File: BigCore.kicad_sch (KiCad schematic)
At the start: 4 parts

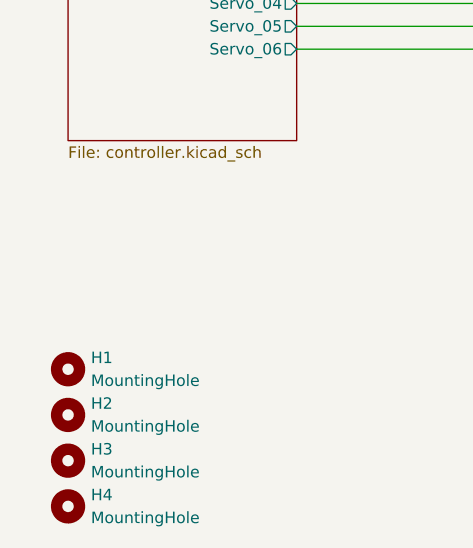
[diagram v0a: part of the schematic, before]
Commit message: Changed the WS2812 driver IC Optimized the Analog GND and AVCC routing Changed RS485 driver Removed TVS Diode at the RS485 driver (already has 15kV rating)
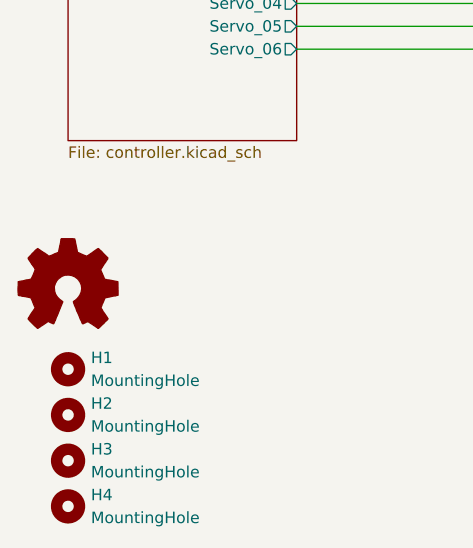
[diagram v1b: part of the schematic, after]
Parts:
- added H5: Logo_Open_Hardware_Small, Symbol:OSHW-Logo_5.7x6mm_SilkScreen, symbol Graphic:Logo_Open_Hardware_Small
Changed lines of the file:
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@@
+	)
+	(symbol
+		(lib_id "Graphic:Logo_Open_Hardware_Small")
+		(at 38.1 156.21 0)
+		(unit 1)
+		(exclude_from_sim no)
+		(in_bom no)
+		(on_board yes)
+		(dnp no)
+		(fields_autoplaced yes)
+		(property "Reference" "H5"
+			(at 38.1 149.225 0)
+			(effects
+				(font
+					(size 1.27 1.27)
+				)
+				(hide yes)
+			)
+		)
+		(property "Value" "Logo_Open_Hardware_Small"
+			(at 38.1 161.925 0)
+			(effects
+				(font
+					(size 1.27 1.27)
+				)
+				(hide yes)
+			)
+		)
+		(property "Footprint" "Symbol:OSHW-Logo_5.7x6mm_SilkScreen"
+			(at 38.1 156.21 0)
+			(effects
+				(font
+					(size 1.27 1.27)
+				)
+				(hide yes)
+			)
+		)
+		(property "Datasheet" "~"
+			(at 38.1 156.21 0)
+			(effects
+				(font
+					(size 1.27 1.27)
+				)
+				(hide yes)
+			)
+		)
+		(property "Description" "Open Hardware logo, small"
+			(at 38.1 156.21 0)
+			(effects
+				(font
+					(size 1.27 1.27)
+				)
+				(hide yes)
+			)
+		)
+		(property "Sim.Enable" "0"
+			(at 38.1 156.21 0)
+			(effects
+				(font
+					(size 1.27 1.27)
+				)
+				(hide yes)
+			)
+		)
+		(instances
+			(project ""
+				(path "/9351c569-8a22-403a-823f-92ee14b5d151"
+					(reference "H5")
+					(unit 1)
+				)
+			)
+		)
 	)
 	(symbol
